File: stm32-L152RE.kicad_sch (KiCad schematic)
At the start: 14 parts, among them SW1 SW_Push, U4 STM32L152RETx

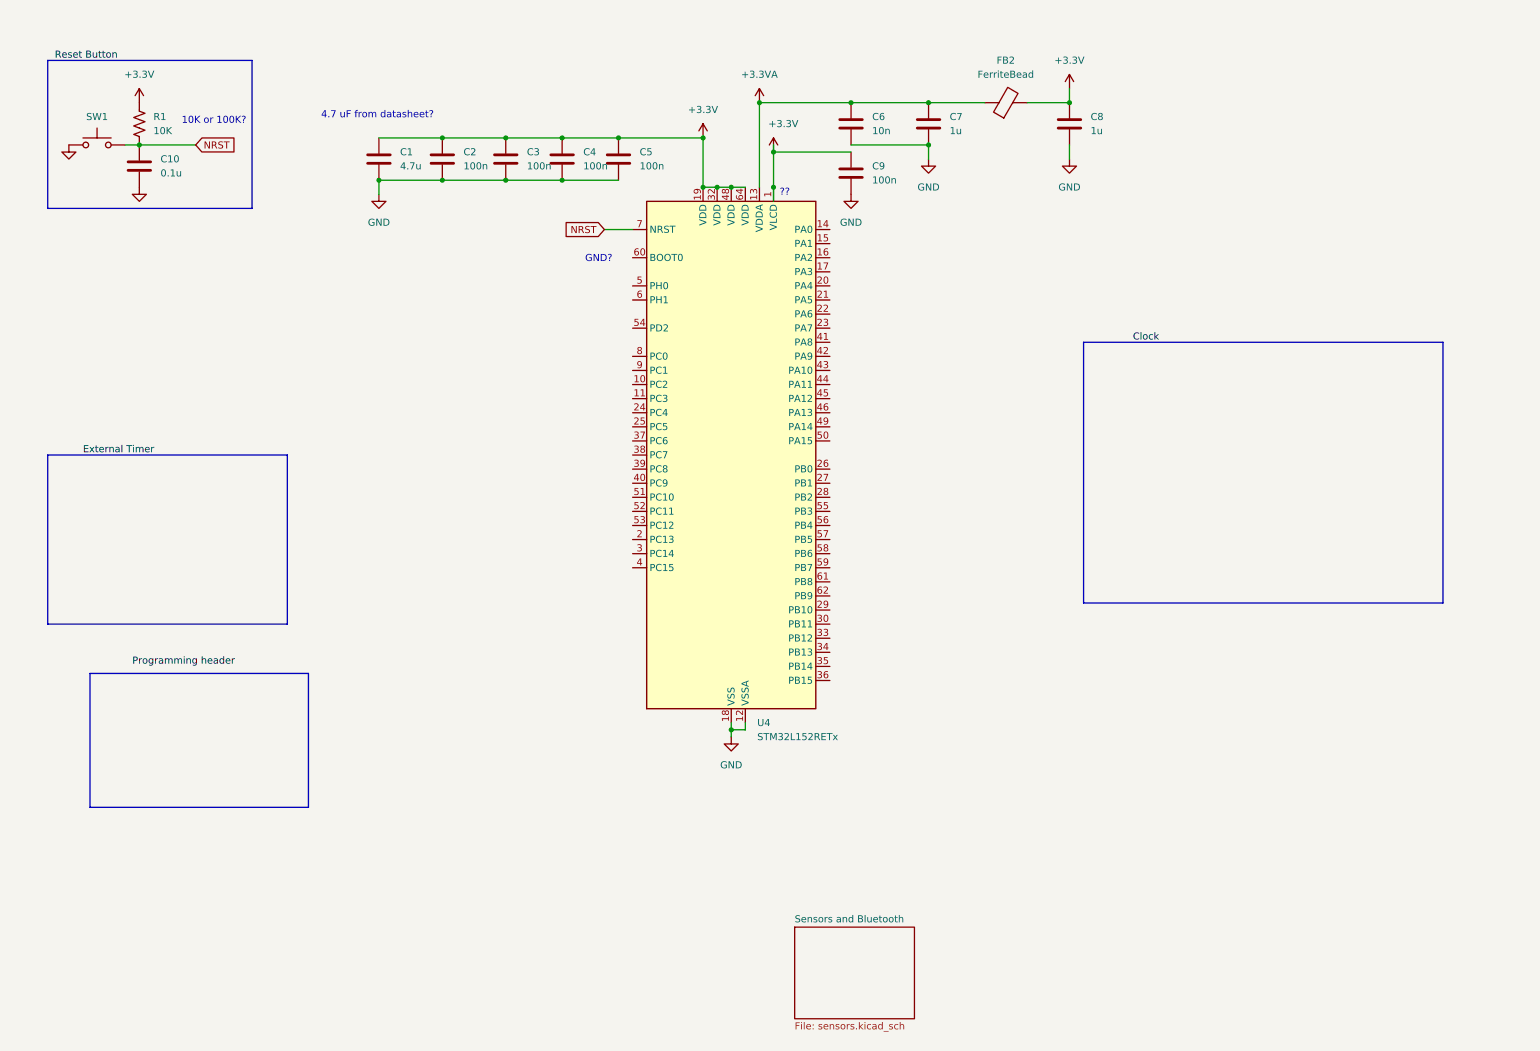
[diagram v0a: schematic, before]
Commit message: oscillator + header + connectors
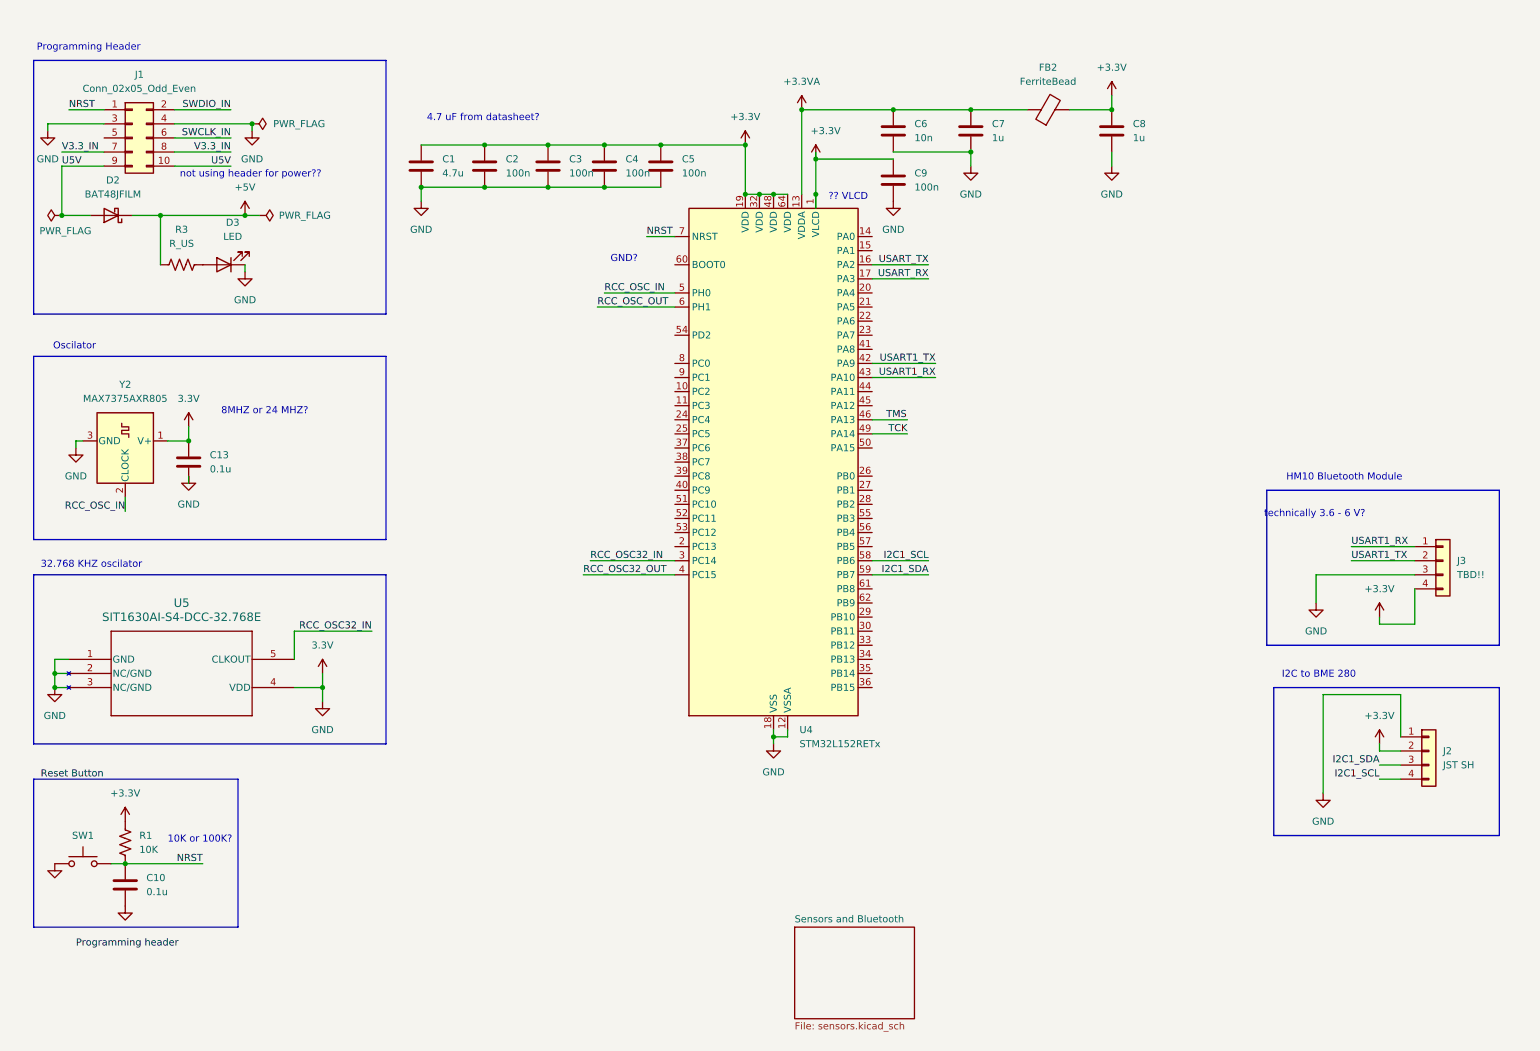
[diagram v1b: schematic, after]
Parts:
- added C13: 0.1u, symbol Device:C
- added D2: BAT48JFILM, Diode_SMD:D_SOD-323, symbol Diode:BAT48JFILM
- added D3: LED, symbol Device:LED
- added J1: Conn_02x05_Odd_Even, Connector_IDC:IDC-Header_2x05_P2.54mm_Latch_Vertical, symbol Connector_Generic:Conn_02x05_Odd_Even
- added J2: JST SH, Connector_JST:JST_SH_BM04B-SRSS-TB_1x04-1MP_P1.00mm_Vertical, symbol Connector_Generic:Conn_01x04
- added J3: TBD!!, symbol Connector_Generic:Conn_01x04
- added R3: R_US, symbol Device:R_US
- added U5: SIT1630AI-S4-DCC-32.768E, FootprintLibrary:SOT_SiT1630-S_SIT, symbol SOT_SiT1630-S_SIT:SIT1630AI-S4-DCC-32.768E
- added Y2: MAX7375AXR805, Package_TO_SOT_SMD:SOT-323_SC-70, symbol Oscillator:MAX7375AXR805
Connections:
- net +3.3V: now also J2.2 (Pin_2), J3.4 (Pin_4)
- net NRST: now also J1.1 (Pin_1)
- net USART_TX: now reaches U4.16 (PA2)
- net USART_RX: now reaches U4.17 (PA3)
- net RCC_OSC32_IN: now reaches U4.3 (PC14)
- net RCC_OSC32_IN: now also U5.5 (CLKOUT)
- net RCC_OSC32_OUT: now reaches U4.4 (PC15)
- net USART1_TX: now reaches U4.42 (PA9)
- net USART1_TX: now also J3.2 (Pin_2)
- net USART1_RX: now reaches U4.43 (PA10)
- net USART1_RX: now also J3.1 (Pin_1)
- net TMS: now reaches U4.46 (PA13)
- net TCK: now reaches U4.49 (PA14)
- net RCC_OSC_IN: now reaches U4.5 (PH0)
- net RCC_OSC_IN: now also Y2.2 (CLOCK)
- net I2C1_SCL: now reaches U4.58 (PB6)
- net I2C1_SCL: now also J2.4 (Pin_4)
- net I2C1_SDA: now reaches U4.59 (PB7)
- net I2C1_SDA: now also J2.3 (Pin_3)
- net RCC_OSC_OUT: now reaches U4.6 (PH1)
- net GND renamed 3.3V
- net 3.3V: now also C13.1, C13.2, D3.1 (K), J1.3 (Pin_3), J1.4 (Pin_4), J2.1 (Pin_1), J3.3 (Pin_3), U5.1 (GND), U5.2 (NC/GND), U5.3 (NC/GND), U5.4 (VDD), Y2.1 (V+), Y2.3 (GND)
- new net: D3.2 (A), R3.2
- new net +5V: D2.1 (K), R3.1
- new net SWCLK_IN: J1.6 (Pin_6)
- new net SWDIO_IN: J1.2 (Pin_2)
- new net U5V: D2.2 (A), J1.10 (Pin_10), J1.9 (Pin_9)
- new net V3.3_IN: J1.7 (Pin_7), J1.8 (Pin_8)
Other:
- note added: "32.768 KHZ oscilator"
- note added: "8MHZ or 24 MHZ?"
- note added: "?? VLCD"
- note added: "HM10 Bluetooth Module"
- note added: "I2C to BME 280"
- note added: "Oscilator"
- note added: "Programming Header"
- note added: "not using header for power??"
- note added: "technically 3.6 - 6 V?"
- note removed: "??"
- moved on the sheet: C1, C10, C2, C3, C4, C5, C6, C7, C8, C9, FB2, R1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

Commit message: analog connection
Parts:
- added J4, J5: TDB, symbol Connector_Generic:Conn_01x03
- added R4, R6: 10k, symbol Device:R_US
- added R5, R7: 14k, symbol Device:R_US
- J1: value Conn_02x05_Odd_Even -> IDC 2x05 2.54mm
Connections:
- net 3.3V is gone; now on net +3.3V: C1.2, C10.2, C13.1, C13.2, C2.2, C3.2, C4.2, C5.2, C6.2, C7.2, C8.2, C9.2, D3.1 (K), J1.3 (Pin_3), J1.4 (Pin_4), J2.1 (Pin_1), J3.3 (Pin_3), SW1.1, U4.12 (VSSA), U4.18 (VSS), U4.31 (VSS), U4.47 (VSS), U4.63 (VSS), U5.1 (GND), U5.2 (NC/GND), U5.3 (NC/GND), U5.4 (VDD), Y2.1 (V+), Y2.3 (GND)
- net SWCLK_IN is gone; now on net TCK: J1.6 (Pin_6)
- net SWDIO_IN is gone; now on net TMS: J1.2 (Pin_2)
- net +3.3V: now also J4.3 (Pin_3), J5.3 (Pin_3), R4.1, R6.1
- net V3.3_IN: no longer names the net of J1.7 (Pin_7)
- net V3.3_IN: no longer J1.8 (Pin_8)
- new net: R6.2, R7.1
- new net: J4.2 (Pin_2), R7.2
- new net: R4.2, R5.1
- new net: J5.2 (Pin_2), R5.2
- new net +12V: J4.1 (Pin_1), J5.1 (Pin_1)
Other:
- note added: "2.54 mm VS 1.27 mm?"
- note added: "8 MHz Oscilator"
- note added: "Anenometer (analog)"
- note added: "To ADC"
- note added: "Wind Dir (analog)"
- note added: "extra SPI"
- note added: "extra i2c"
- note removed: "8MHZ or 24 MHZ?"
- note removed: "Oscilator"
- moved on the sheet: C10, C13, D2, D3, J1, R1, R3, SW1, U5, Y2

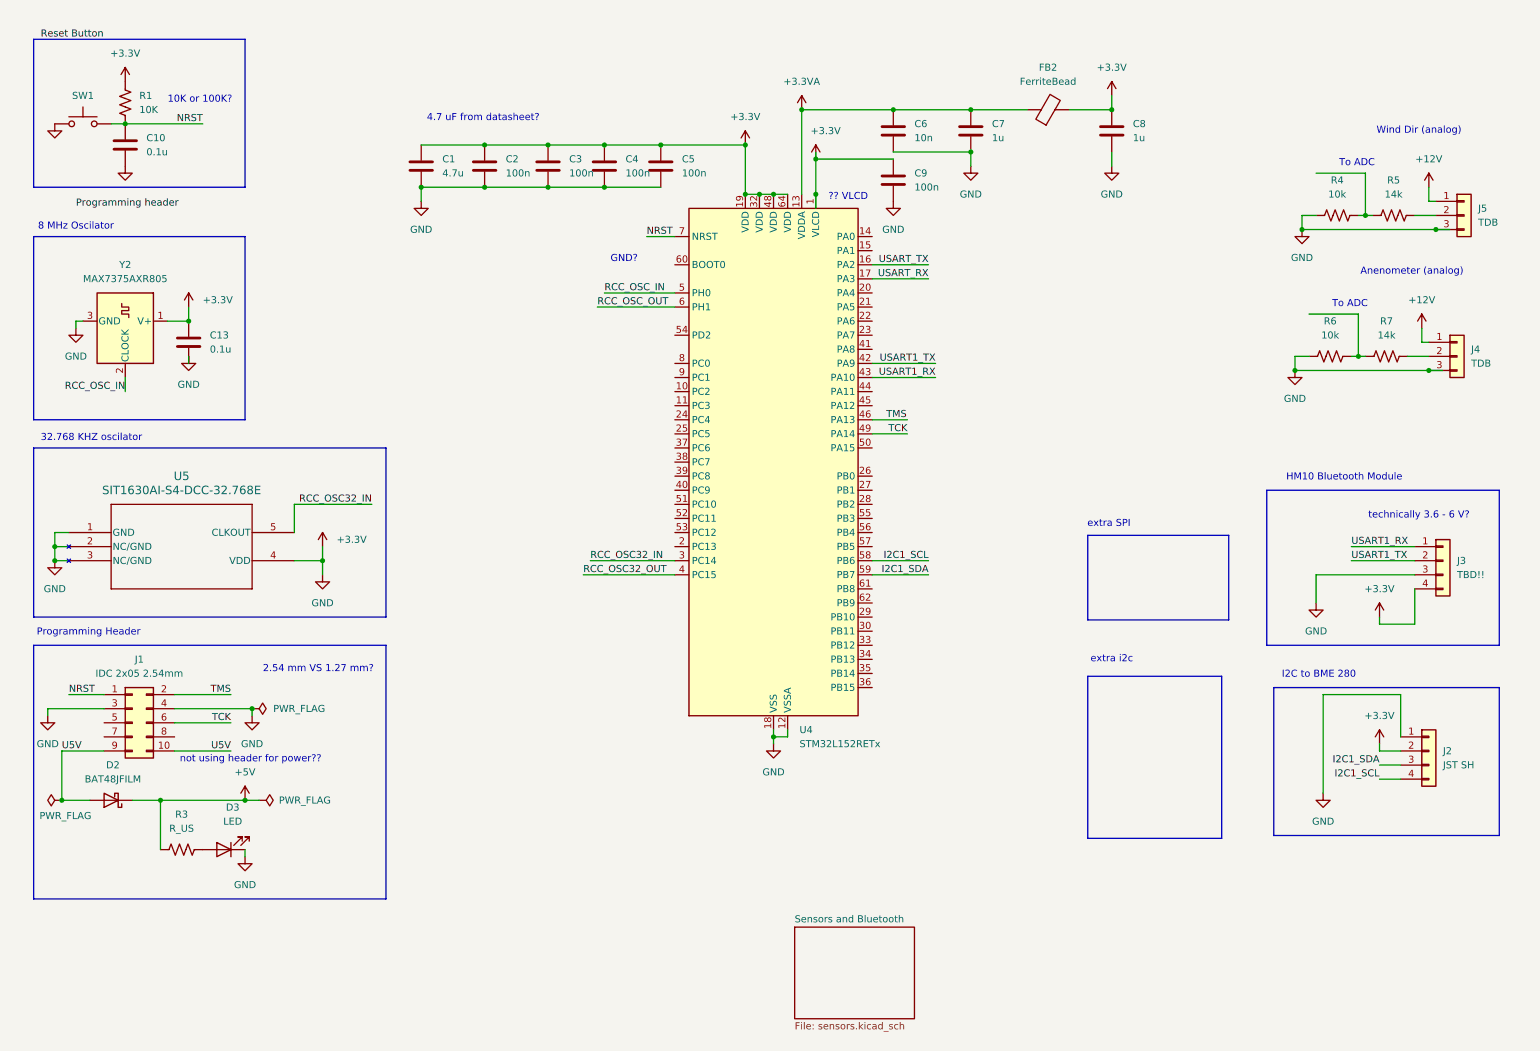
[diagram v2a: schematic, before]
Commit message: add buck
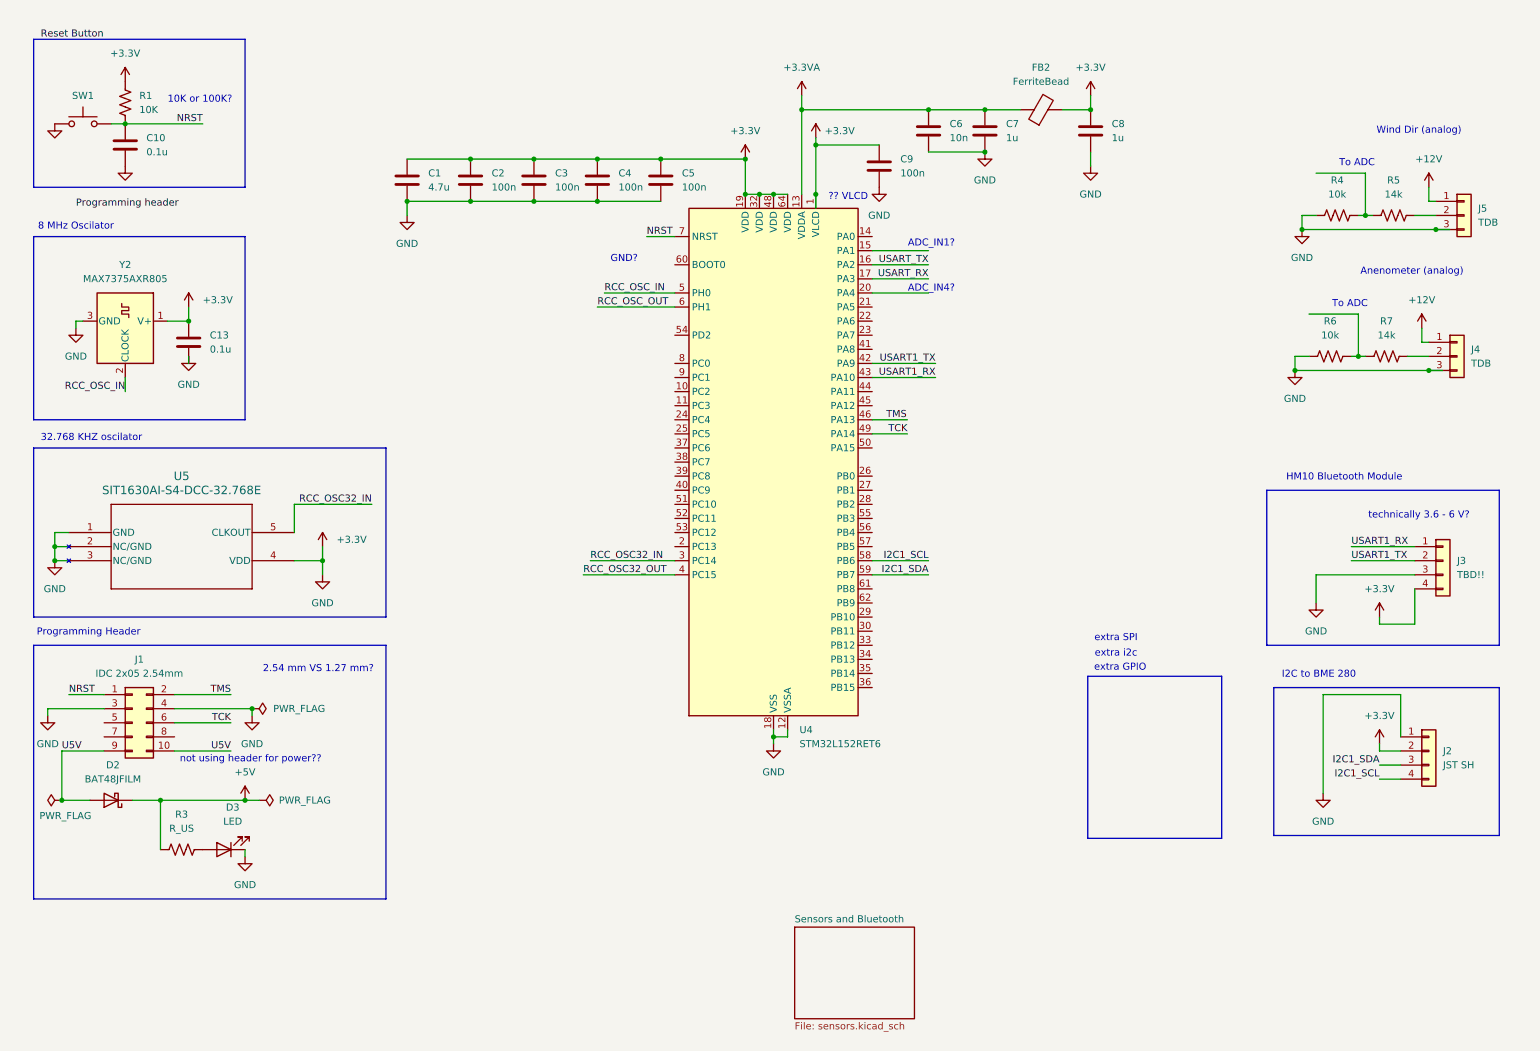
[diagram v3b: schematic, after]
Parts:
- U4: value STM32L152RETx -> STM32L152RET6
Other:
- note added: "ADC_IN1?"
- note added: "ADC_IN4?"
- note added: "extra GPIO"
- note removed: "4.7 uF from datasheet?"
- moved on the sheet: C1, C2, C3, C4, C5, C6, C7, C8, C9, FB2

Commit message: Add files via upload
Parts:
- removed D2: BAT48JFILM, Diode_SMD:D_SOD-323, symbol Diode:BAT48JFILM
- removed D3: LED, symbol Device:LED
- removed J1: IDC 2x05 2.54mm, Connector_IDC:IDC-Header_2x05_P2.54mm_Latch_Vertical, symbol Connector_Generic:Conn_02x05_Odd_Even
- removed J3: TBD!!, symbol Connector_Generic:Conn_01x04
- removed R3: R_US, symbol Device:R_US
- added J1: Conn_01x04_Pin, symbol Connector:Conn_01x04_Pin
- added J6: IDC 2x05 2.54mm, Connector_IDC:IDC-Header_2x05_P2.54mm_Latch_Vertical, symbol Connector_Generic:Conn_02x05_Odd_Even
- added J7: Conn_01x02_Pin, symbol Connector:Conn_01x02_Pin
- added R12, R13: 4.7k, symbol Device:R_US
- added R14: 100k, symbol Device:R_US
- renumbered C10 to C12, C6 to C14, C7 to C15, C8 to C16, C1 to C17, C2 to C18, C3 to C19, C4 to C20, C5 to C21, C9 to C22, R6 to R10, R7 to R11, R1 to R7, R4 to R8, R5 to R9
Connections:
- net +3.3V: now also J1.1 (Pin_1), J1.2 (Pin_2), J6.4 (Pin_4), R14.1; no longer U5.2 (NC/GND), U5.3 (NC/GND)
- net I2C1_SCL: now also R12.1
- net I2C1_SDA: now also R13.1
- net USART1_RX: now also J1.4 (Pin_4)
- net USART1_TX: now also J1.3 (Pin_3)
- net USART_RX: now also J7.2 (Pin_2)
- net USART_TX: now also J7.1 (Pin_1)
- net ADC_IN4: now reaches R10.2, R11.1
- net ADC_IN4: now also U4.20 (PA4)
- net ADC_IN1: now reaches R8.2, R9.1
- net ADC_IN1: now also U4.15 (PA1)
- net at U4.60 (BOOT0): now also R14.2
- net TCK renamed SWCLK
- net SWCLK: now also J6.6 (Pin_6)
- net TMS renamed SWDIO
- net SWDIO: now also J6.2 (Pin_2)
- new net: R12.2, R13.2
- no-connect marks 0 -> 46
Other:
- removed sheet Sensors and Bluetooth
- note added: "3.3V"
- note added: "5V"
- note added: "BME280"
- note added: "GND"
- note added: "Microcontorller"
- note added: "RST"
- note added: "Reset Button"
- note added: "ST LINK Programming Header"
- note added: "SWIM"
- note added: "need to add: extra GPIO status LEDS debug connection points"
- note added: "needs diodes??"
- note removed: "ADC_IN1?"
- note removed: "ADC_IN4?"
- note removed: "GND?"
- note removed: "I2C to BME 280"
- note removed: "Programming Header"
- note removed: "To ADC"
- note removed: "extra GPIO"
- note removed: "extra SPI"
- note removed: "extra i2c"
- note removed: "not using header for power??"
- note removed: "technically 3.6 - 6 V?"
- title: STM32L152RE, Programming Header etc  -> STM32L152RE Dev Board
- moved on the sheet: C12, C13, C14, C15, C16, C17, C18, C19, C20, C21, C22, FB2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
